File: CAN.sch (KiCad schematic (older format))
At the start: 6 parts, among them IC4 ADUM3054, U5 AP1117-50

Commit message: - rescued schematic - added *.sch-bak to ignore - fixed bypass diode polarity - fixed PDEN being low - added 0R resistors instead of USB iso option - added caps to DCDC - added filter to VDDA
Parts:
- C11, C12, C9: symbol Device:C_Small -> HSWR-V2-rescue:C_Small-Device
- IC4: symbol HSWR-V2-rescue:ADUM3054-Auktoralib -> HSWR-V2-rescue:ADUM3054-Auktoralib-HSWR-rescue
- R30: symbol Device:R_Small -> HSWR-V2-rescue:R_Small-Device
- U5: symbol Regulator_Linear:AP1117-50 -> HSWR-V2-rescue:AP1117-50-Regulator_Linear
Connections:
- no-connect marks 0 -> 1
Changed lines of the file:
@@
 EESchema Schematic File Version 4
-LIBS:HSWR V2-cache
-EELAYER 26 0
+EELAYER 30 0
 EELAYER END
 $Descr A4 11693 8268
@@
 CANL
 $Comp
-L Device:C_Small C9
+L HSWR-V2-rescue:C_Small-Device C9
 U 1 1 5759CF39
 P 5700 2600
@@
 $EndComp
 $Comp
-L Device:C_Small C11
+L HSWR-V2-rescue:C_Small-Device C11
 U 1 1 5759D08A
 P 4350 2600
@@
 $EndComp
 $Comp
-L power:Earth #PWR029
+L HSWR-V2-rescue:Earth-power #PWR029
 U 1 1 5759DCFE
 P 4650 2800
@@
 $EndComp
 $Comp
-L power:GND #PWR032
+L HSWR-V2-rescue:GND-power #PWR032
 U 1 1 5759E8F5
 P 6050 4050
@@
 $EndComp
 $Comp
-L Device:R_Small R30
+L HSWR-V2-rescue:R_Small-Device R30
 U 1 1 5759ED7A
 P 5350 3250
@@
 V+Sense
 $Comp
-L Device:C_Small C12
+L HSWR-V2-rescue:C_Small-Device C12
 U 1 1 575A0498
 P 6200 2600
@@
 $EndComp
 $Comp
-L power:+3V3 #PWR033
+L HSWR-V2-rescue:+3V3-power #PWR033
 U 1 1 575A0BC8
 P 6200 2500
@@
 $EndComp
 $Comp
-L power:Earth #PWR0115
+L HSWR-V2-rescue:Earth-power #PWR0115
 U 1 1 5CA085F6
 P 5700 2700
@@
 $EndComp
 $Comp
-L Regulator_Linear:AP1117-50 U5
+L HSWR-V2-rescue:AP1117-50-Regulator_Linear U5
 U 1 1 5CA08F00
 P 4650 2500
@@
 $EndComp
 $Comp
-L power:Earth #PWR0167
+L HSWR-V2-rescue:Earth-power #PWR0167
 U 1 1 5CA09500
 P 4350 2800
@@
 Wire Wire Line
 	5700 2500 5850 2500
-Connection ~ 5350 3150
-Connection ~ 5350 3350
-$Comp
-L HSWR-V2-rescue:ADUM3054-Auktoralib IC4
+$Comp
+L HSWR-V2-rescue:ADUM3054-Auktoralib-HSWR-rescue IC4
 U 1 1 5CA06D6C
 P 5950 3400
@@
 $EndComp
 $Comp
-L power:Earth #PWR0168
+L HSWR-V2-rescue:Earth-power #PWR0168
 U 1 1 5CA09CBC
 P 5750 4050
@@
 $EndComp
 $Comp
-L power:Earth #PWR0169
+L HSWR-V2-rescue:Earth-power #PWR0169
 U 1 1 5CA09D7B
 P 5850 4050
@@
 $EndComp
 $Comp
-L power:GND #PWR0170
+L HSWR-V2-rescue:GND-power #PWR0170
 U 1 1 5CA0A130
 P 6150 4050
@@
 $EndComp
 $Comp
-L power:GND #PWR0171
+L HSWR-V2-rescue:GND-power #PWR0171
 U 1 1 5CA0A147
 P 6250 4050
@@
 $EndComp
 $Comp
-L power:GND #PWR0172
+L HSWR-V2-rescue:GND-power #PWR0172
 U 1 1 5CA0A1E2
 P 6200 2700
@@
 Connection ~ 6200 2500
 $Comp
-L power:+12VA #PWR0199
+L HSWR-V2-rescue:+12VA-power #PWR0199
 U 1 1 5C9EF966
 P 4350 2500
@@
 $EndComp
 Connection ~ 4350 2500
+NoConn ~ 5350 3550
 $EndSCHEMATC

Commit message: - changed CSA for Hall effect sensors - updated power stage layout
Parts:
- renumbered C11 to C52, C9 to C53, C12 to C54, R30 to R40, U5 to U8
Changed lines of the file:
@@
 CANL
 $Comp
-L HSWR-V2-rescue:C_Small-Device C9
+L HSWR-V2-rescue:C_Small-Device C53
 U 1 1 5759CF39
 P 5700 2600
-F 0 "C9" H 5800 2600 50  0000 L CNN
+F 0 "C53" H 5800 2600 50  0000 L CNN
 F 1 "100n" H 5750 2500 50  0000 L CNN
 F 2 "Capacitor_SMD:C_0805_2012Metric" H 5700 2600 60  0001 C CNN
@@
 $EndComp
 $Comp
-L HSWR-V2-rescue:C_Small-Device C11
+L HSWR-V2-rescue:C_Small-Device C52
 U 1 1 5759D08A
 P 4350 2600
-F 0 "C11" H 4500 2600 50  0000 L CNN
+F 0 "C52" H 4500 2600 50  0000 L CNN
 F 1 "100n" H 4450 2500 50  0000 L CNN
 F 2 "Capacitor_SMD:C_0805_2012Metric" H 4350 2600 60  0001 C CNN
@@
 $EndComp
 $Comp
-L HSWR-V2-rescue:Earth-power #PWR029
+L HSWR-V2-rescue:Earth-power #PWR0102
 U 1 1 5759DCFE
 P 4650 2800
-F 0 "#PWR029" H 4650 2550 50  0001 C CNN
+F 0 "#PWR0102" H 4650 2550 50  0001 C CNN
 F 1 "Earth" H 4650 2650 50  0001 C CNN
 F 2 "" H 4650 2800 60  0000 C CNN
@@
 $EndComp
 $Comp
-L HSWR-V2-rescue:GND-power #PWR032
+L HSWR-V2-rescue:GND-power #PWR0106
 U 1 1 5759E8F5
 P 6050 4050
-F 0 "#PWR032" H 6050 3800 50  0001 C CNN
+F 0 "#PWR0106" H 6050 3800 50  0001 C CNN
 F 1 "GND" H 6050 3900 50  0000 C CNN
 F 2 "" H 6050 4050 60  0000 C CNN
@@
 $EndComp
 $Comp
-L HSWR-V2-rescue:R_Small-Device R30
+L HSWR-V2-rescue:R_Small-Device R40
 U 1 1 5759ED7A
 P 5350 3250
-F 0 "R30" V 5250 3200 50  0000 L CNN
+F 0 "R40" V 5250 3200 50  0000 L CNN
 F 1 "120R" H 5400 3250 50  0000 L CNN
 F 2 "Resistor_SMD:R_0805_2012Metric" H 5350 3250 60  0001 C CNN
@@
 V+Sense
 $Comp
-L HSWR-V2-rescue:C_Small-Device C12
+L HSWR-V2-rescue:C_Small-Device C54
 U 1 1 575A0498
 P 6200 2600
-F 0 "C12" H 6350 2600 50  0000 L CNN
+F 0 "C54" H 6350 2600 50  0000 L CNN
 F 1 "100n" H 6300 2500 50  0000 L CNN
 F 2 "Capacitor_SMD:C_0805_2012Metric" H 6200 2600 60  0001 C CNN
@@
 $EndComp
 $Comp
-L HSWR-V2-rescue:+3V3-power #PWR033
+L HSWR-V2-rescue:+3V3-power #PWR0108
 U 1 1 575A0BC8
 P 6200 2500
-F 0 "#PWR033" H 6200 2350 50  0001 C CNN
+F 0 "#PWR0108" H 6200 2350 50  0001 C CNN
 F 1 "+3V3" H 6200 2640 50  0000 C CNN
 F 2 "" H 6200 2500 60  0000 C CNN
@@
 $EndComp
 $Comp
-L HSWR-V2-rescue:Earth-power #PWR0115
+L HSWR-V2-rescue:Earth-power #PWR0103
 U 1 1 5CA085F6
 P 5700 2700
-F 0 "#PWR0115" H 5700 2450 50  0001 C CNN
+F 0 "#PWR0103" H 5700 2450 50  0001 C CNN
 F 1 "Earth" H 5700 2550 50  0001 C CNN
 F 2 "" H 5700 2700 60  0000 C CNN
@@
 $EndComp
 $Comp
-L HSWR-V2-rescue:AP1117-50-Regulator_Linear U5
+L HSWR-V2-rescue:AP1117-50-Regulator_Linear U8
 U 1 1 5CA08F00
 P 4650 2500
-F 0 "U5" H 4650 2742 50  0000 C CNN
+F 0 "U8" H 4650 2742 50  0000 C CNN
 F 1 "AP1117-50" H 4650 2651 50  0000 C CNN
 F 2 "Package_TO_SOT_SMD:SOT-223-3_TabPin2" H 4650 2700 50  0001 C CNN
@@
 $EndComp
 $Comp
-L HSWR-V2-rescue:Earth-power #PWR0167
+L HSWR-V2-rescue:Earth-power #PWR0101
 U 1 1 5CA09500
 P 4350 2800
-F 0 "#PWR0167" H 4350 2550 50  0001 C CNN
+F 0 "#PWR0101" H 4350 2550 50  0001 C CNN
 F 1 "Earth" H 4350 2650 50  0001 C CNN
 F 2 "" H 4350 2800 60  0000 C CNN
@@
 	5700 2500 5850 2500
 $Comp
-L HSWR-V2-rescue:ADUM3054-Auktoralib-HSWR-rescue IC4
+L HSWR-V2-rescue:ADUM3054-Auktoralib-HSWR-rescue IC?
 U 1 1 5CA06D6C
 P 5950 3400
-AR Path="/5CA06D6C" Ref="IC4"  Part="1"
+AR Path="/5CA06D6C" Ref="IC?"  Part="1"
 AR Path="/5899E225/5CA06D6C" Ref="IC4"  Part="1"
 F 0 "IC4" H 5500 2850 50  0000 C CNN
@@
 $EndComp
 $Comp
-L HSWR-V2-rescue:Earth-power #PWR0168
+L HSWR-V2-rescue:Earth-power #PWR0104
 U 1 1 5CA09CBC
 P 5750 4050
-F 0 "#PWR0168" H 5750 3800 50  0001 C CNN
+F 0 "#PWR0104" H 5750 3800 50  0001 C CNN
 F 1 "Earth" H 5750 3900 50  0001 C CNN
 F 2 "" H 5750 4050 60  0000 C CNN
@@
 $EndComp
 $Comp
-L HSWR-V2-rescue:Earth-power #PWR0169
+L HSWR-V2-rescue:Earth-power #PWR0105
 U 1 1 5CA09D7B
 P 5850 4050
-F 0 "#PWR0169" H 5850 3800 50  0001 C CNN
+F 0 "#PWR0105" H 5850 3800 50  0001 C CNN
 F 1 "Earth" H 5850 3900 50  0001 C CNN
 F 2 "" H 5850 4050 60  0000 C CNN
@@
 $EndComp
 $Comp
-L HSWR-V2-rescue:GND-power #PWR0170
+L HSWR-V2-rescue:GND-power #PWR0107
 U 1 1 5CA0A130
 P 6150 4050
-F 0 "#PWR0170" H 6150 3800 50  0001 C CNN
+F 0 "#PWR0107" H 6150 3800 50  0001 C CNN
 F 1 "GND" H 6150 3850 50  0000 C CNN
 F 2 "" H 6150 4050 60  0000 C CNN
@@
 $EndComp
 $Comp
-L HSWR-V2-rescue:GND-power #PWR0171
+L HSWR-V2-rescue:GND-power #PWR0110
 U 1 1 5CA0A147
 P 6250 4050
-F 0 "#PWR0171" H 6250 3800 50  0001 C CNN
+F 0 "#PWR0110" H 6250 3800 50  0001 C CNN
 F 1 "GND" H 6250 3900 50  0000 C CNN
 F 2 "" H 6250 4050 60  0000 C CNN
@@
 $EndComp
 $Comp
-L HSWR-V2-rescue:GND-power #PWR0172
+L HSWR-V2-rescue:GND-power #PWR0109
 U 1 1 5CA0A1E2
 P 6200 2700
-F 0 "#PWR0172" H 6200 2450 50  0001 C CNN
+F 0 "#PWR0109" H 6200 2450 50  0001 C CNN
 F 1 "GND" H 6200 2550 50  0000 C CNN
 F 2 "" H 6200 2700 60  0000 C CNN
@@
 Connection ~ 6200 2500
 $Comp
-L HSWR-V2-rescue:+12VA-power #PWR0199
+L HSWR-V2-rescue:+12VA-power #PWR0100
 U 1 1 5C9EF966
 P 4350 2500
-F 0 "#PWR0199" H 4350 2350 50  0001 C CNN
+F 0 "#PWR0100" H 4350 2350 50  0001 C CNN
 F 1 "+12VA" H 4365 2673 50  0000 C CNN
 F 2 "" H 4350 2500 50  0001 C CNN

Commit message: - removed rescue lib and symbols - added HSWR.lib
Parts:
- C52, C53, C54: symbol HSWR-V2-rescue:C_Small-Device -> Device:C_Small
- IC4: symbol HSWR-V2-rescue:ADUM3054-Auktoralib-HSWR-rescue -> HSWR:ADUM3054
- R40: symbol HSWR-V2-rescue:R_Small-Device -> Device:R_Small
- U8: symbol HSWR-V2-rescue:AP1117-50-Regulator_Linear -> HSWR:AP1117-50
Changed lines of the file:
@@
 $Descr A4 11693 8268
 encoding utf-8
-Sheet 7 8
+Sheet 6 8
 Title "HSWR CAN Transceiver"
 Date "2017-02-05"
@@
 CANL
 $Comp
-L HSWR-V2-rescue:C_Small-Device C53
+L Device:C_Small C53
 U 1 1 5759CF39
 P 5700 2600
@@
 $EndComp
 $Comp
-L HSWR-V2-rescue:C_Small-Device C52
+L Device:C_Small C52
 U 1 1 5759D08A
 P 4350 2600
@@
 $EndComp
 $Comp
-L HSWR-V2-rescue:Earth-power #PWR0102
+L power:Earth #PWR0102
 U 1 1 5759DCFE
 P 4650 2800
@@
 $EndComp
 $Comp
-L HSWR-V2-rescue:GND-power #PWR0106
+L power:GND #PWR0106
 U 1 1 5759E8F5
 P 6050 4050
@@
 $EndComp
 $Comp
-L HSWR-V2-rescue:R_Small-Device R40
+L Device:R_Small R40
 U 1 1 5759ED7A
 P 5350 3250
@@
 V+Sense
 $Comp
-L HSWR-V2-rescue:C_Small-Device C54
+L Device:C_Small C54
 U 1 1 575A0498
 P 6200 2600
@@
 $EndComp
 $Comp
-L HSWR-V2-rescue:+3V3-power #PWR0108
+L power:+3V3 #PWR0108
 U 1 1 575A0BC8
 P 6200 2500
@@
 $EndComp
 $Comp
-L HSWR-V2-rescue:Earth-power #PWR0103
+L power:Earth #PWR0103
 U 1 1 5CA085F6
 P 5700 2700
@@
 $EndComp
 $Comp
-L HSWR-V2-rescue:AP1117-50-Regulator_Linear U8
+L HSWR:AP1117-50 U8
 U 1 1 5CA08F00
 P 4650 2500
@@
 $EndComp
 $Comp
-L HSWR-V2-rescue:Earth-power #PWR0101
+L power:Earth #PWR0101
 U 1 1 5CA09500
 P 4350 2800
@@
 	4350 2800 4350 2700
 Wire Wire Line
-	4950 2500 5700 2500
-Wire Wire Line
 	5850 2500 5850 2750
-Connection ~ 5700 2500
-Wire Wire Line
-	5700 2500 5850 2500
-$Comp
-L HSWR-V2-rescue:ADUM3054-Auktoralib-HSWR-rescue IC?
+$Comp
+L HSWR:ADUM3054 IC?
 U 1 1 5CA06D6C
 P 5950 3400
@@
 $EndComp
 $Comp
-L HSWR-V2-rescue:Earth-power #PWR0104
+L power:Earth #PWR0104
 U 1 1 5CA09CBC
 P 5750 4050
@@
 $EndComp
 $Comp
-L HSWR-V2-rescue:Earth-power #PWR0105
+L power:Earth #PWR0105
 U 1 1 5CA09D7B
 P 5850 4050
@@
 $EndComp
 $Comp
-L HSWR-V2-rescue:GND-power #PWR0107
+L power:GND #PWR0107
 U 1 1 5CA0A130
 P 6150 4050
@@
 $EndComp
 $Comp
-L HSWR-V2-rescue:GND-power #PWR0110
+L power:GND #PWR0110
 U 1 1 5CA0A147
 P 6250 4050
@@
 $EndComp
 $Comp
-L HSWR-V2-rescue:GND-power #PWR0109
+L power:GND #PWR0109
 U 1 1 5CA0A1E2
 P 6200 2700
@@
 Wire Wire Line
 	6050 2500 6200 2500
-Connection ~ 6200 2500
-$Comp
-L HSWR-V2-rescue:+12VA-power #PWR0100
+$Comp
+L power:+12VA #PWR0100
 U 1 1 5C9EF966
 P 4350 2500
@@
 	1    0    0    -1
 $EndComp
+NoConn ~ 5350 3550
+Wire Wire Line
+	4950 2500 5700 2500
+Connection ~ 5350 3150
+Connection ~ 5350 3350
+Connection ~ 6200 2500
+Connection ~ 5700 2500
+Wire Wire Line
+	5700 2500 5850 2500
 Connection ~ 4350 2500
-NoConn ~ 5350 3550
 $EndSCHEMATC

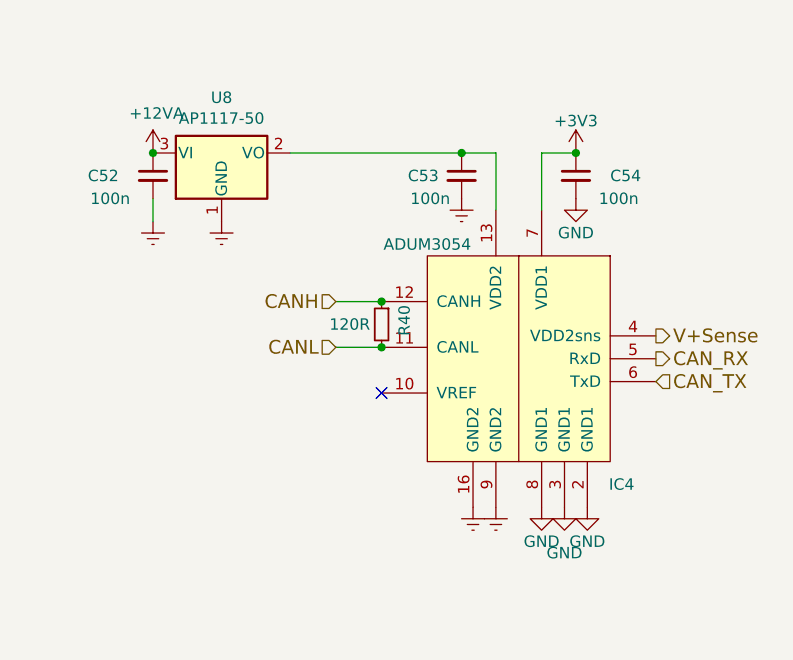
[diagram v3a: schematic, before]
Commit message: - reworked IO section -> now fully isolated - added fan output - sensor IO is now differential - exposed differential UART interface - fan pin not defined yet!
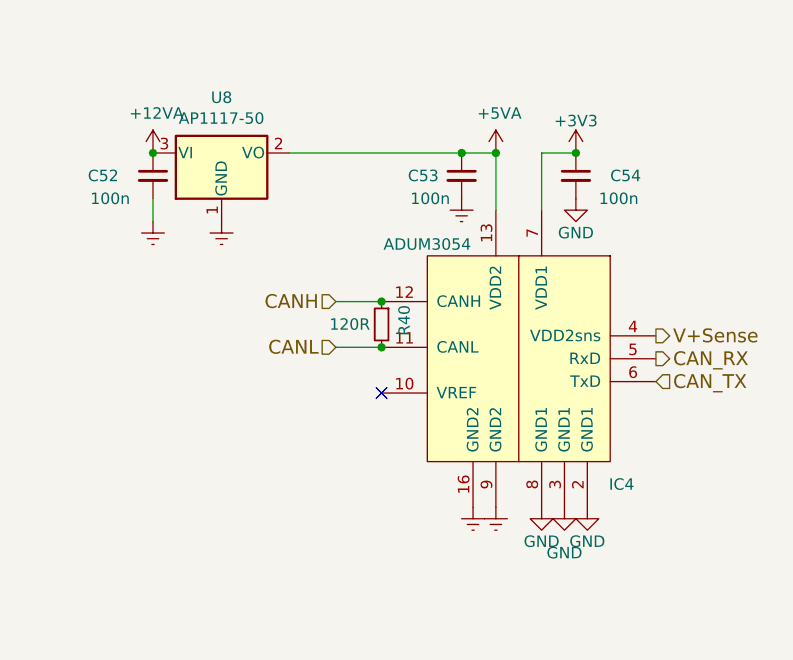
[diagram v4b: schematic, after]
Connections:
- net +5VA: now reaches C53.1, IC4.13 (VDD2), U8.2 (VO)
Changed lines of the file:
@@
 EESchema Schematic File Version 4
+LIBS:HSWR-cache
 EELAYER 30 0
 EELAYER END
@@
 $EndComp
 NoConn ~ 5350 3550
-Wire Wire Line
-	4950 2500 5700 2500
 Connection ~ 5350 3150
 Connection ~ 5350 3350
@@
 	5700 2500 5850 2500
 Connection ~ 4350 2500
+Wire Wire Line
+	4950 2500 5700 2500
+$Comp
+L power:+5VA #PWR0144
+U 1 1 5E5C760E
+P 5850 2500
+F 0 "#PWR0144" H 5850 2350 50  0001 C CNN
+F 1 "+5VA" H 5865 2673 50  0000 C CNN
+F 2 "" H 5850 2500 50  0001 C CNN
+F 3 "" H 5850 2500 50  0001 C CNN
+	1    5850 2500
+	1    0    0    -1
+$EndComp
+Connection ~ 5850 2500
 $EndSCHEMATC

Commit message: - removed some unused symbols from HSWR.lib - changed U8 (linear reg) to standard symbol - fixed wrong footprint for C24
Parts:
- removed U8: AP1117-50, Package_TO_SOT_SMD:SOT-223-3_TabPin2, symbol HSWR:AP1117-50
- added U8: AP1117-50, Package_TO_SOT_SMD:SOT-223-3_TabPin2, symbol Regulator_Linear:AP1117-50
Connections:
- net +12VA: now also U8.3 (VI)
- net +5VA: now also U8.2 (VO)
- net Earth: now also U8.1 (GND)
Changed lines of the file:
@@
-$EndComp
-$Comp
-L HSWR:AP1117-50 U8
-U 1 1 5CA08F00
-P 4650 2500
-F 0 "U8" H 4650 2742 50  0000 C CNN
-F 1 "AP1117-50" H 4650 2651 50  0000 C CNN
-F 2 "Package_TO_SOT_SMD:SOT-223-3_TabPin2" H 4650 2700 50  0001 C CNN
-F 3 "http://www.diodes.com/datasheets/AP1117.pdf" H 4750 2250 50  0001 C CNN
-	1    4650 2500
-	1    0    0    -1
 $EndComp
 $Comp
@@
 Wire Wire Line
 	5700 2500 5850 2500
-Connection ~ 4350 2500
 Wire Wire Line
 	4950 2500 5700 2500
@@
 $EndComp
 Connection ~ 5850 2500
+$Comp
+L Regulator_Linear:AP1117-50 U8
+U 1 1 5E613077
+P 4650 2500
+F 0 "U8" H 4650 2742 50  0000 C CNN
+F 1 "AP1117-50" H 4650 2651 50  0000 C CNN
+F 2 "Package_TO_SOT_SMD:SOT-223-3_TabPin2" H 4650 2700 50  0001 C CNN
+F 3 "http://www.diodes.com/datasheets/AP1117.pdf" H 4750 2250 50  0001 C CNN
+	1    4650 2500
+	1    0    0    -1
+$EndComp
+Connection ~ 4350 2500
 $EndSCHEMATC
